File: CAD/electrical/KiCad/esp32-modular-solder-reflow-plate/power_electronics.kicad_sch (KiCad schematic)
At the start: 16 parts, among them J1 PJ-037B, J3 TB003-500-P02BE, Q1 PJD25N06A_L2_00001, U1 LD1117S33TR_SOT223

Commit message: - CAD: schematic improvements
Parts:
- removed C1: 865080545012, library_manager:CAPAE660X770N, symbol library_loader:865080545012
- removed C2, C4: 100nF, Capacitor_SMD:C_0603_1608Metric, symbol Device:C
- removed C5: 10uF, Capacitor_SMD:C_0603_1608Metric, symbol Device:C
- removed C7: 1nF, Capacitor_SMD:C_0805_2012Metric, symbol Device:C
- removed D1, D5: ESDL4151MX4T5G, library_manager:ESDL4151MX4T5G, symbol library_loader:ESDL4151MX4T5G
- removed D2: RRD07MM4STR, Diode_SMD:D_SOD-123, symbol Device:D
- removed J1: PJ-037B, library_manager:PJ037B, symbol library_loader:PJ-037B
- removed J3: TB003-500-P02BE, library_manager:SHDR2W100P0X500_1X2_1000X780X1030P, symbol library_loader:TB003-500-P02BE
- removed Q1: PJD25N06A_L2_00001, library_manager:PJD25N06A_L2_00001, symbol library_loader:PJD25N06A_L2_00001
- removed R1: 4k7, Resistor_SMD:R_0603_1608Metric, symbol Device:R
- removed R2: 1k, Resistor_SMD:R_0603_1608Metric, symbol Device:R
- removed R4: 10k, Resistor_SMD:R_0603_1608Metric, symbol Device:R
- removed U1: LD1117S33TR_SOT223, Package_TO_SOT_SMD:SOT-223-3_TabPin2, symbol Regulator_Linear:LD1117S33TR_SOT223
- removed Z1: BZT52C24-E3-08, library_manager:BZT52C24E308, symbol library_loader:BZT52C24-E3-08
- added C17, C18, C20, C21, C24: 100n, symbol Device:C_Small
- added C19: 470µ, symbol Device:C_Polarized_Small
- added C23: 47µ, symbol Device:C_Small
- added D11, D9: Flyback, symbol Device:D_Schottky
- added D13: D_TVS, symbol Device:D_TVS
- added D8: Rev. Pol., symbol Device:LED_Small
- added F1: 1.5A, symbol Device:Fuse_Small
- added L2: L_Ferrite_Small, symbol Device:L_Ferrite_Small
- added Q2: Heater N-FET, symbol Device:Q_NMOS_DGS
- added Q3: Q_PMOS_DGS, symbol Device:Q_PMOS_DGS
- added R25: 330, symbol Device:R_Small
- added U5: AMS1117-3.3, Package_TO_SOT_SMD:SOT-223-3_TabPin2, symbol Regulator_Linear:AMS1117-3.3
- added U6: AMS1117-5.0, Package_TO_SOT_SMD:SOT-223-3_TabPin2, symbol Regulator_Linear:AMS1117-5.0
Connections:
- net +3V3: now also C18.1, U5.2 (VO)
- net GND: now also C17.2, C18.2, C19.2, C20.2, C21.2, C23.2, C24.2, D13.1 (A1), Q2.3 (S), Q3.2 (G), R25.2, U5.1 (GND), U6.1 (GND)
- new net: F1.1, Q3.3 (S)
- new net: D8.2 (A), R25.1
- new net: C24.1, D9.2 (A), U6.2 (VO)
- new net +5V: D9.1 (K)
- new net HEATER_CTRL: Q2.2 (G)
- new net HEATER_N: D11.2 (A), Q2.1 (D)
- new net HEATER_P: C17.1, C19.1, C23.1, D11.1 (K), F1.2, L2.1
- new net PWR_IN_P: D13.2 (A2), D8.1 (K), Q3.1 (D)
- new net VBUS: C20.1, C21.1, L2.2, U5.3 (VI), U6.3 (VI)
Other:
- note added: "LDOs"
- note added: "Power-Input"
- note removed: "3.3V LDO and filtering"
- note removed: "Power, Pre-filtering, Voltage divider"
- title: (none) -> Modular Solder Reflow PCB

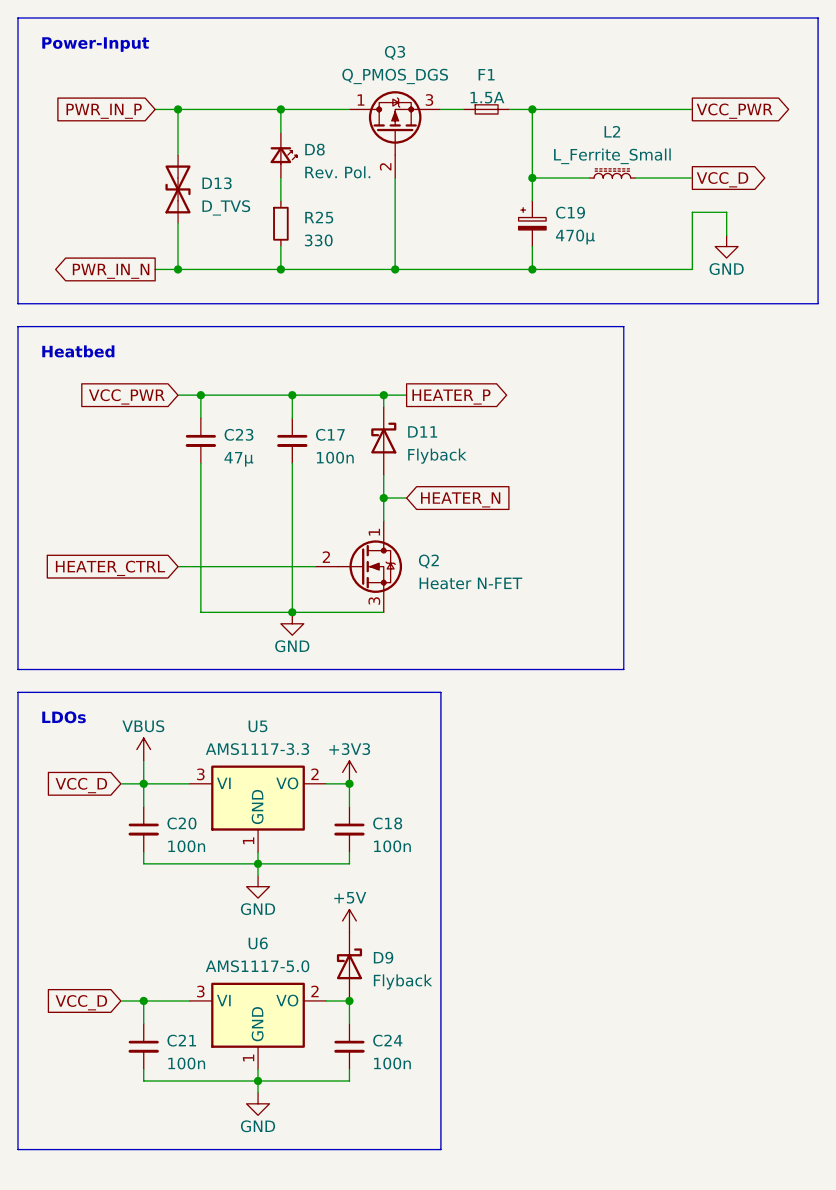
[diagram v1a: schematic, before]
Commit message: - CAD: initial routed pcb
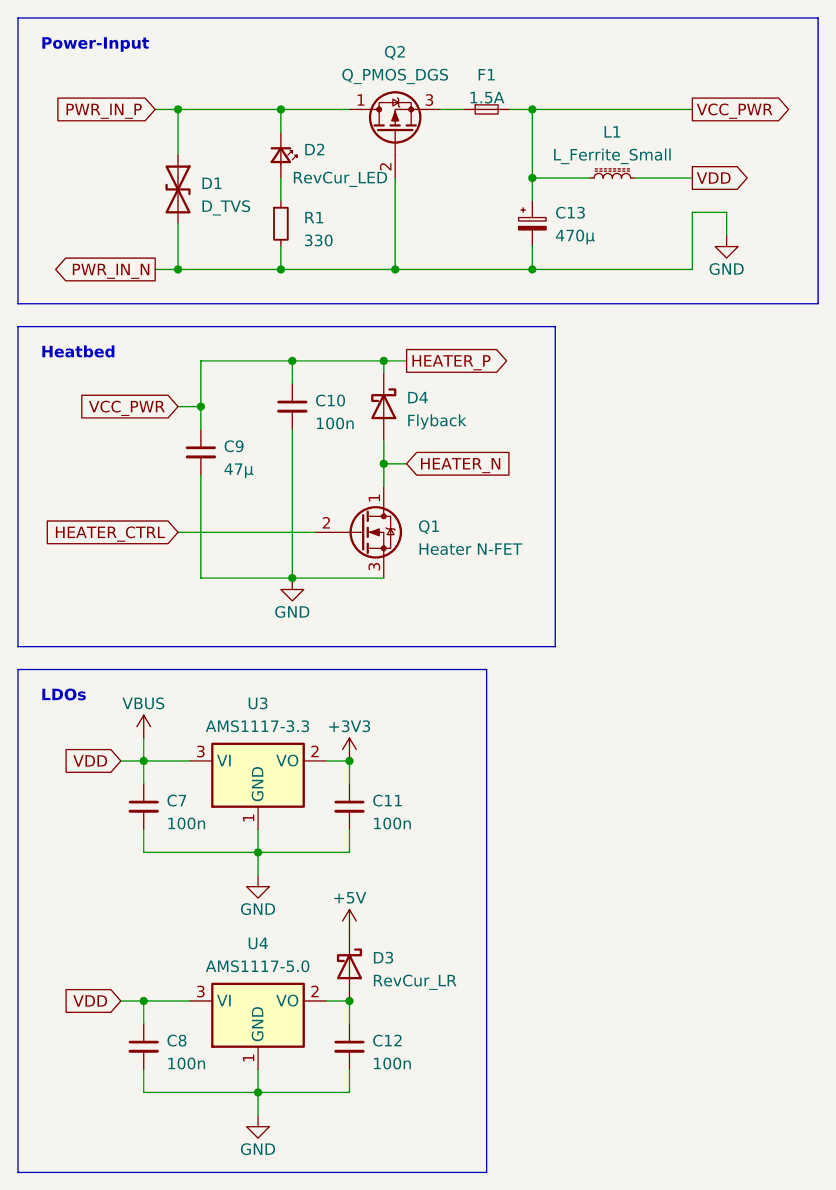
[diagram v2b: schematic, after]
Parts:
- C10: renamed from C17; footprint (none) -> Capacitor_SMD:C_0603_1608Metric_Pad1.08x0.95mm_HandSolder
- C11: renamed from C18; footprint (none) -> Capacitor_SMD:C_0603_1608Metric_Pad1.08x0.95mm_HandSolder
- C12: renamed from C24; footprint (none) -> Capacitor_SMD:C_0603_1608Metric_Pad1.08x0.95mm_HandSolder
- C13: renamed from C19; footprint (none) -> Capacitor_THT:CP_Radial_D6.3mm_P2.50mm
- C7: renamed from C20; footprint (none) -> Capacitor_SMD:C_0603_1608Metric_Pad1.08x0.95mm_HandSolder
- C8: renamed from C21; footprint (none) -> Capacitor_SMD:C_0603_1608Metric_Pad1.08x0.95mm_HandSolder
- C9: renamed from C23; footprint (none) -> Capacitor_SMD:C_0603_1608Metric_Pad1.08x0.95mm_HandSolder
- D1: renamed from D13; footprint (none) -> Diode_SMD:D_0603_1608Metric_Pad1.05x0.95mm_HandSolder
- D2: renamed from D8; value Rev. Pol. -> RevCur_LED; footprint (none) -> LED_SMD:LED_0603_1608Metric_Pad1.05x0.95mm_HandSolder
- D3: renamed from D9; value Flyback -> RevCur_LR; footprint (none) -> Diode_SMD:D_1210_3225Metric_Pad1.42x2.65mm_HandSolder
- D4: renamed from D11; footprint (none) -> Diode_SMD:D_1210_3225Metric_Pad1.42x2.65mm_HandSolder
- F1: footprint (none) -> Fuse:Fuseholder_Cylinder-5x20mm_Schurter_0031_8201_Horizontal_Open
- L1: renamed from L2; footprint (none) -> Inductor_SMD:L_0805_2012Metric_Pad1.15x1.40mm_HandSolder
- Q1: renamed from Q2; footprint (none) -> Package_TO_SOT_SMD:ATPAK-2
- Q2: renamed from Q3; footprint (none) -> Package_TO_SOT_SMD:ATPAK-2
- R1: renamed from R25; footprint (none) -> Resistor_SMD:R_0603_1608Metric_Pad0.98x0.95mm_HandSolder
- renumbered U5 to U3, U6 to U4
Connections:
- net GND: now also D1.2 (A2); no longer D1.1 (A1)
- net PWR_IN_P: now also D1.1 (A1); no longer D1.2 (A2)
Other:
- moved on the sheet: C10, C11, C7, C9, D1, D4, Q1, U3

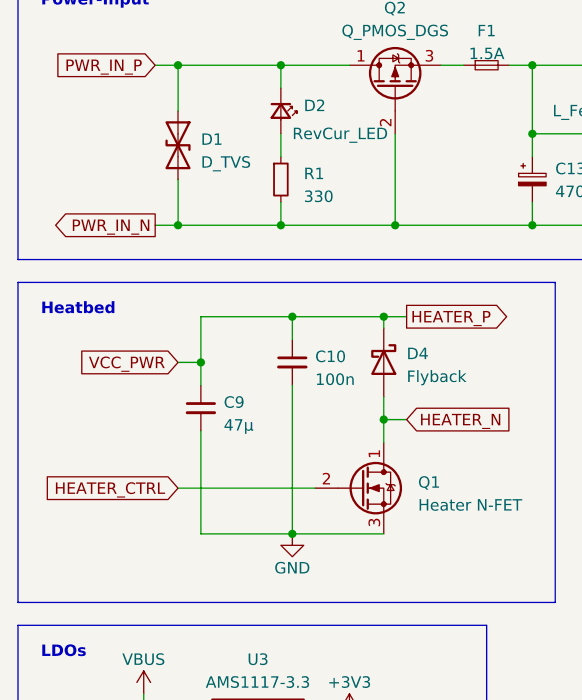
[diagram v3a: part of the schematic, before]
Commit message: - cad: improved routing; added VIN voltage monitoring capability
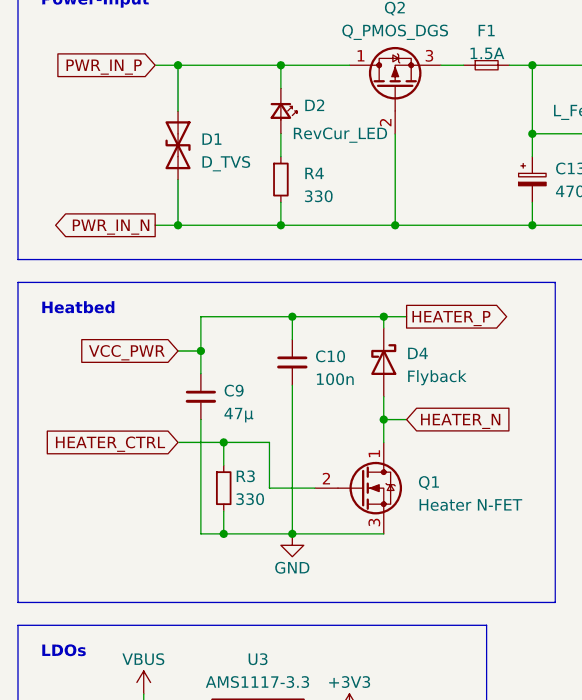
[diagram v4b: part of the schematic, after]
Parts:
- added R3: 330, Resistor_SMD:R_0603_1608Metric_Pad0.98x0.95mm_HandSolder, symbol Device:R_Small
- renumbered R1 to R4
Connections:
- net GND: now also R3.2
- net HEATER_CTRL: now also R3.1
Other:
- moved on the sheet: C9

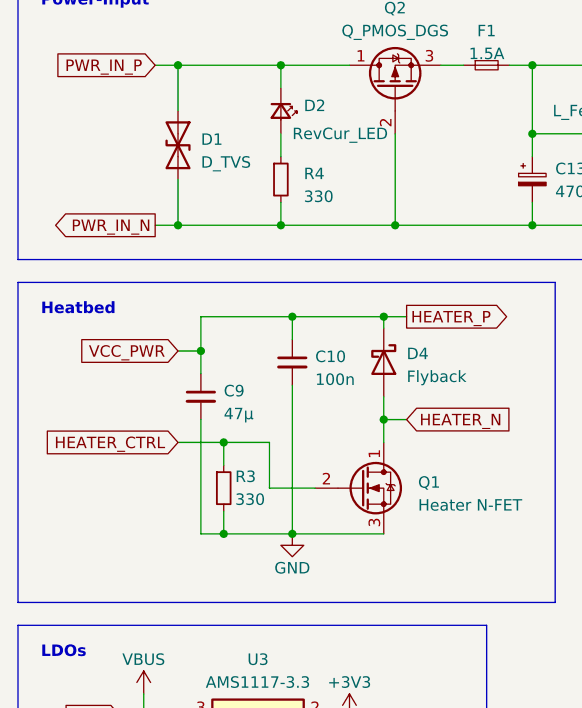
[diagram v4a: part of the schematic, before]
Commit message: - cad: added a buzzer control output
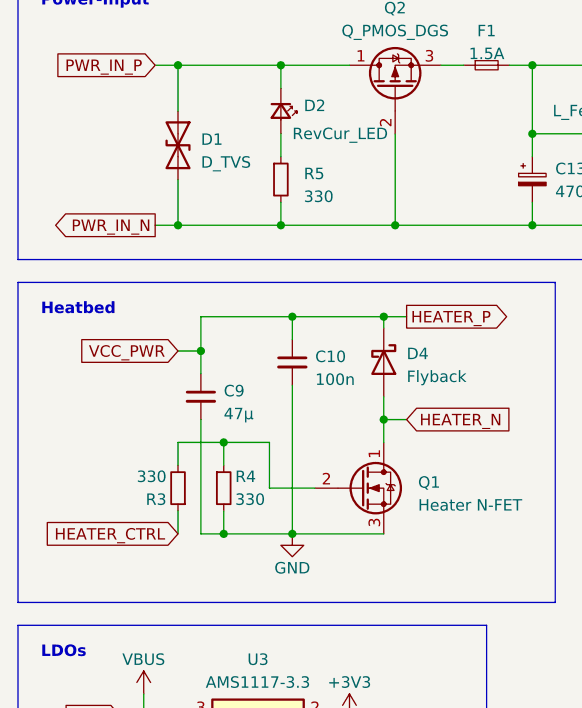
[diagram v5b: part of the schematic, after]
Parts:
- added R3: 330, Resistor_SMD:R_0603_1608Metric_Pad0.98x0.95mm_HandSolder, symbol Device:R_Small
- renumbered R3 to R4, R4 to R5
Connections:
- net HEATER_CTRL: now also R3.1; no longer Q1.2 (G), R4.1
- new net: Q1.2 (G), R3.2, R4.1
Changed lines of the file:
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@@
+    (stroke (width 0) (type default))
+  )
+  (wire (pts (xy 33.02 67.31) (xy 33.02 69.85))
     (stroke (width 0) (type default))
   )
@@
   )
   (wire (pts (xy 35.56 53.34) (xy 45.72 53.34))
+    (stroke (width 0) (type default))
+  )
+  (wire (pts (xy 33.02 74.93) (xy 33.02 77.47))
     (stroke (width 0) (type default))
   )
@@
     )
   )
-  (global_label "HEATER_CTRL" (shape input) (at 33.02 67.31 180) (fields_autoplaced)
+  (global_label "HEATER_CTRL" (shape input) (at 33.02 77.47 180) (fields_autoplaced)
     (effects (font (size 1.27 1.27)) (justify right))
-    (property "Intersheetrefs" "${INTERSHEET_REFS}" (at 17.6562 67.31 0)
+    (property "Intersheetrefs" "${INTERSHEET_REFS}" (at 17.6562 77.47 0)
       (effects (font (size 1.27 1.27)) (justify right) hide)
     )
@@
     )
   )
+  (symbol (lib_id "Device:R_Small") (at 33.02 72.39 180) (unit 1)
+    (in_bom yes) (on_board yes) (dnp no)
+    (property "Reference" "R3" (at 31.75 73.66 0)
+      (effects (font (size 1.27 1.27)) (justify left))
+    )
+    (property "Value" "330" (at 31.75 71.12 0)
+      (effects (font (size 1.27 1.27)) (justify left))
+    )
+    (property "Footprint" "Resistor_SMD:R_0603_1608Metric_Pad0.98x0.95mm_HandSolder" (at 33.02 72.39 0)
+      (effects (font (size 1.27 1.27)) hide)
+    )
+    (property "Datasheet" "~" (at 33.02 72.39 0)
+      (effects (font (size 1.27 1.27)) hide)
+    )
+    (pin "1")
+    (pin "2")
+    (instances
+      (project "esp32-modular-solder-reflow-plate"
+        (path "/33f3a99a-8df0-41a5-be2d-1e3400ca68bb/e7c4b288-cae6-41f4-8e83-3e14eed6f49f"
+          (reference "R3") (unit 1)
+        )
+      )
+    )
+  )
   (symbol (lib_id "Device:Q_NMOS_DGS") (at 53.34 72.39 0) (unit 1)
     (in_bom yes) (on_board yes) (dnp no) (fields_autoplaced)
@@
   (symbol (lib_id "Device:R_Small") (at 44.45 38.1 0) (unit 1)
     (in_bom yes) (on_board yes) (dnp no)
-    (property "Reference" "R4" (at 46.99 37.465 0)
+    (property "Reference" "R5" (at 46.99 37.465 0)
       (effects (font (size 1.27 1.27)) (justify left))
     )
@@
       (project "esp32-modular-solder-reflow-plate"
         (path "/33f3a99a-8df0-41a5-be2d-1e3400ca68bb/e7c4b288-cae6-41f4-8e83-3e14eed6f49f"
-          (reference "R4") (unit 1)
+          (reference "R5") (unit 1)
         )
       )
@@
   (symbol (lib_id "Device:R_Small") (at 38.1 72.39 0) (unit 1)
     (in_bom yes) (on_board yes) (dnp no)
-    (property "Reference" "R3" (at 39.37 71.12 0)
+    (property "Reference" "R4" (at 39.37 71.12 0)
       (effects (font (size 1.27 1.27)) (justify left))
     )
@@
       (project "esp32-modular-solder-reflow-plate"
         (path "/33f3a99a-8df0-41a5-be2d-1e3400ca68bb/e7c4b288-cae6-41f4-8e83-3e14eed6f49f"
-          (reference "R3") (unit 1)
-        )
-      )
+          (reference "R4") (unit 1)
+        )
+      )

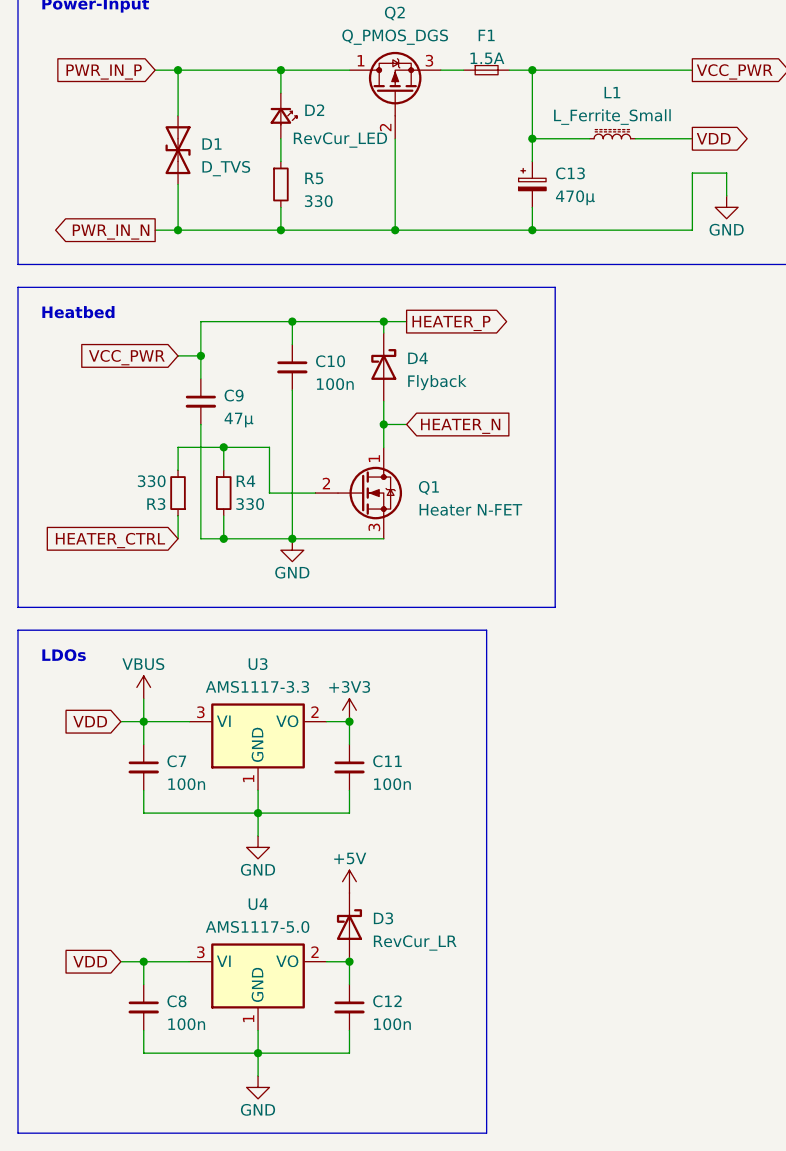
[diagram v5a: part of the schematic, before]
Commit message: - cad: add an auxiliary temperature probe input
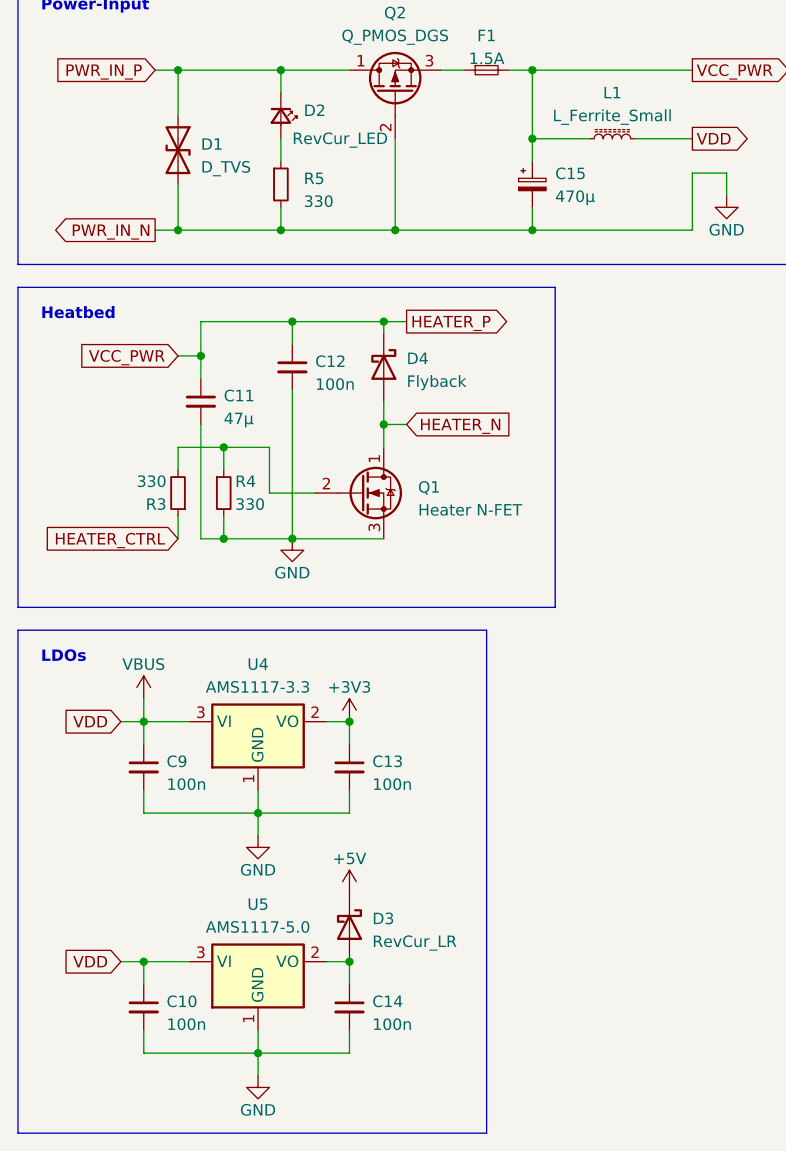
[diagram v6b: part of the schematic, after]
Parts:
- renumbered C8 to C10, C9 to C11, C10 to C12, C11 to C13, C12 to C14, C13 to C15, C7 to C9, U3 to U4, U4 to U5
